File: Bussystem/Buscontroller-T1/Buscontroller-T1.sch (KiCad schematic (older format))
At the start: 14 parts, among them J1 PCIE-098-edge-conn, J2 Conn_01x02_Female, J3 J1B1211CCD, U1 LM7805L-TF3-T, U2 Teensy4.1

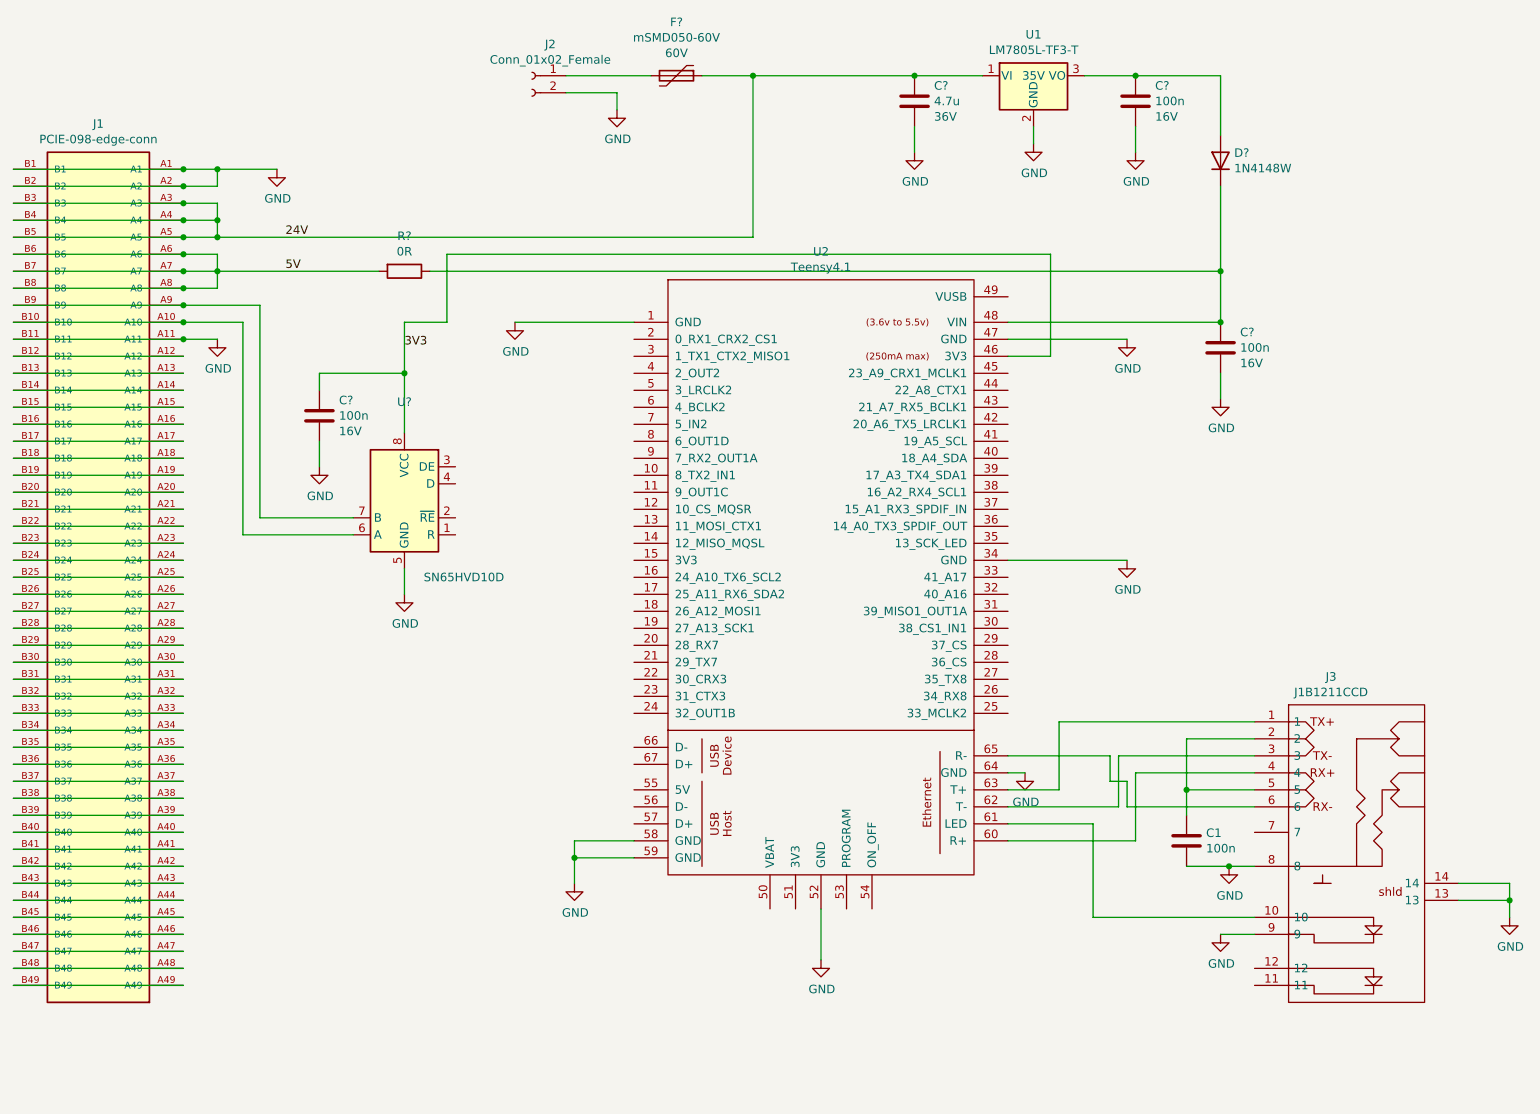
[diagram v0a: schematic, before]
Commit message: some new parts in the Buscontroller T1
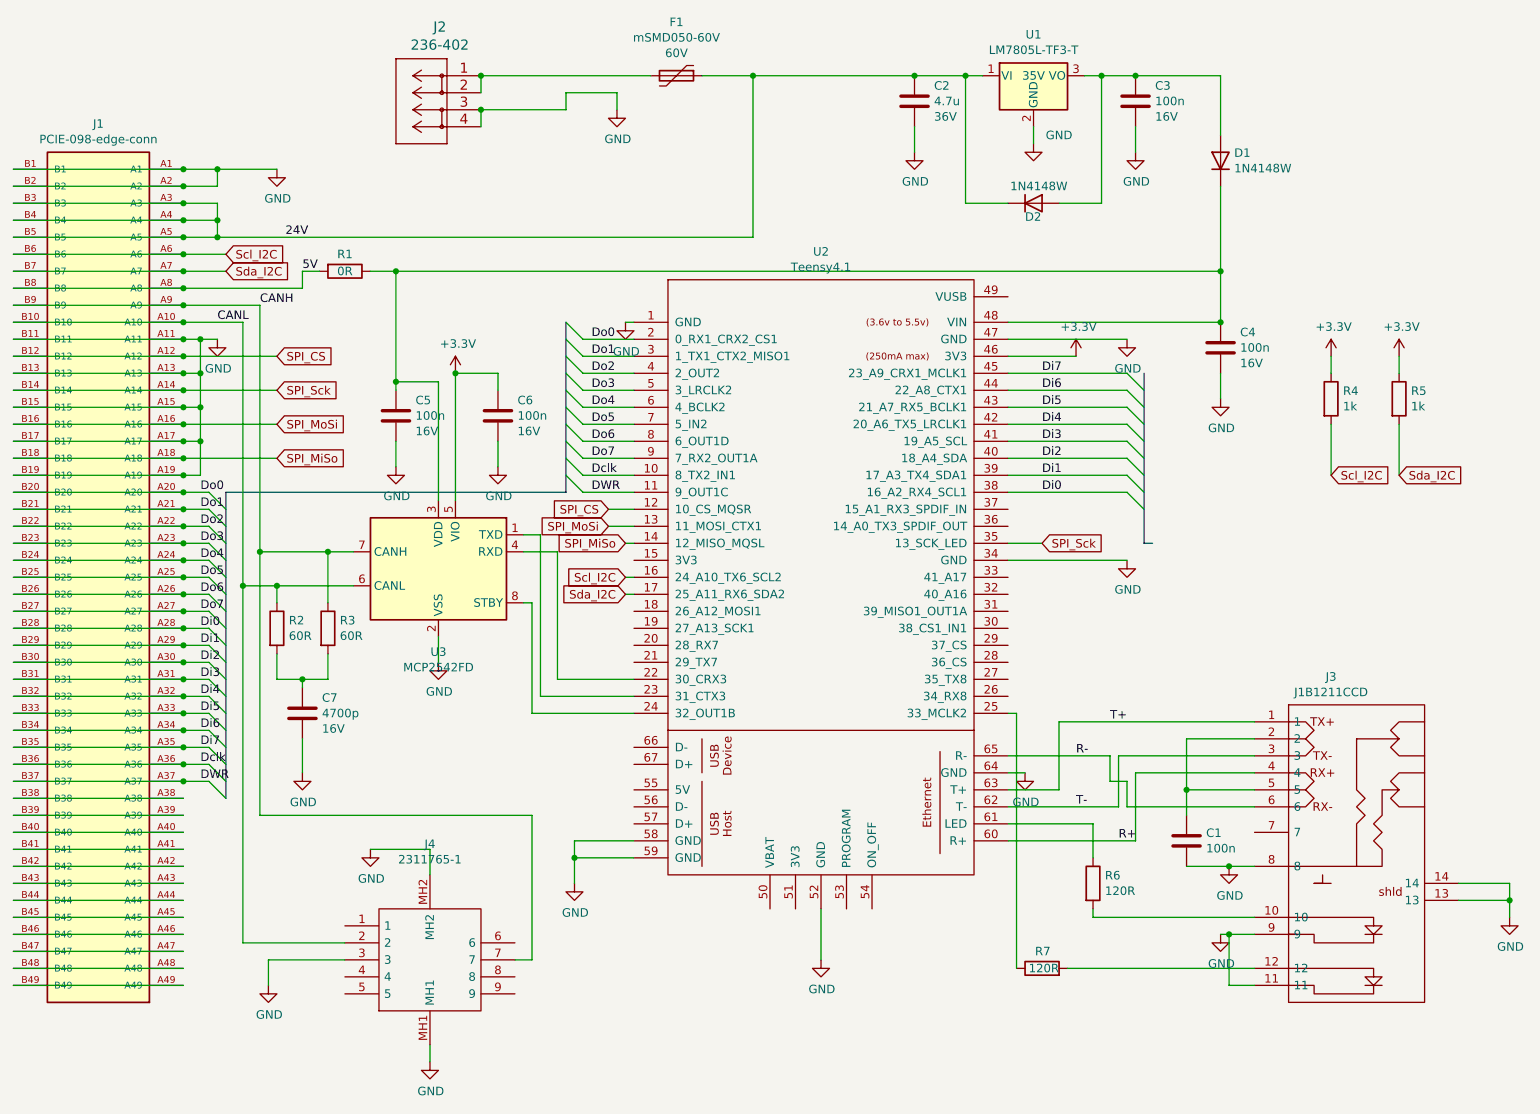
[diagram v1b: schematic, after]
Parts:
- removed J2: Conn_01x02_Female, footprints:236-402, symbol Connector:Conn_01x02_Female
- removed U?: SN65HVD10D, Package_SO:SOIC-8_3.9x4.9mm_P1.27mm, symbol Interface_UART:SN65LBC176D
- added C5: 100n, Capacitors_SMD:C_0805_HandSoldering, symbol Device:C
- added C7: 4700p, Capacitors_SMD:C_0805_HandSoldering, symbol Device:C
- added D2: 1N4148W, Diodes_SMD:D_SOD-123, symbol Device:D
- added J2: 236-402, footprints:236-402, symbol 2021-07-08_17-54-53:236-402
- added J4: 2311765-1, 23117651, symbol SamacSys_Parts:2311765-1
- added R2, R3: 60R, Resistors_SMD:R_0603_HandSoldering, symbol Device:R
- added R4, R5: 1k, Resistors_SMD:R_0603_HandSoldering, symbol Device:R
- added R6, R7: 120R, Resistors_SMD:R_0603_HandSoldering, symbol Device:R
- added U3: MCP2542FD, Housings_SOIC:SOIC-8-1EP_3.9x4.9mm_Pitch1.27mm, symbol Interface_CAN_LIN:MCP2542FDxMF
- gave numbers to parts that had none: 7
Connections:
- net 24V: now also D2.1 (K)
- net 5V: no longer J1.A6, J1.A7, J1.B6, J1.B7
- net GND: now also J1.A13, J1.A15, J1.A17, J1.A19, J1.B13, J1.B15, J1.B17, J1.B19, J3.11, C5.2, C7.2, J2.3, J2.4, J4.3, J4.MH1, J4.MH2, U3.2 (VSS), U3.9 (VSS)
- net CANL: now reaches J1.A10, J1.B10
- net CANL: now also J4.2, R2.1, U3.6 (CANL)
- net SPI_CS: now reaches J1.A12, J1.B12
- net SPI_CS: now also U2.12 (10_CS_MQSR)
- net SPI_Sck: now reaches J1.A14, J1.B14
- net SPI_Sck: now also U2.35 (13_SCK_LED)
- net SPI_MoSi: now reaches J1.A16, J1.B16
- net SPI_MoSi: now also U2.13 (11_MOSI_CTX1)
- net SPI_MiSo: now reaches J1.A18, J1.B18
- net SPI_MiSo: now also U2.14 (12_MISO_MQSL)
- net Do0: now reaches J1.A20, J1.B20
- net Do0: now also U2.2 (0_RX1_CRX2_CS1)
- net Do1: now reaches J1.A21, J1.B21
- net Do1: now also U2.3 (1_TX1_CTX2_MISO1)
- net Do2: now reaches J1.A22, J1.B22
- net Do2: now also U2.4 (2_OUT2)
- net Do3: now reaches J1.A23, J1.B23
- net Do3: now also U2.5 (3_LRCLK2)
- net Do4: now reaches J1.A24, J1.B24
- net Do4: now also U2.6 (4_BCLK2)
- net Do5: now reaches J1.A25, J1.B25
- net Do5: now also U2.7 (5_IN2)
- net Do6: now reaches J1.A26, J1.B26
- net Do6: now also U2.8 (6_OUT1D)
- net Do7: now reaches J1.A27, J1.B27
- net Do7: now also U2.9 (7_RX2_OUT1A)
- net Di0: now reaches J1.A28, J1.B28
- net Di0: now also U2.38 (16_A2_RX4_SCL1)
- net Di1: now reaches J1.A29, J1.B29
- net Di1: now also U2.39 (17_A3_TX4_SDA1)
- net Di2: now reaches J1.A30, J1.B30
- net Di2: now also U2.40 (18_A4_SDA)
- net Di3: now reaches J1.A31, J1.B31
- net Di3: now also U2.41 (19_A5_SCL)
- net Di4: now reaches J1.A32, J1.B32
- net Di4: now also U2.42 (20_A6_TX5_LRCLK1)
- net Di5: now reaches J1.A33, J1.B33
- net Di5: now also U2.43 (21_A7_RX5_BCLK1)
- net Di6: now reaches J1.A34, J1.B34
- net Di6: now also U2.44 (22_A8_CTX1)
- net Di7: now reaches J1.A35, J1.B35
- net Di7: now also U2.45 (23_A9_CRX1_MCLK1)
- net Dclk: now reaches J1.A36, J1.B36
- net Dclk: now also U2.10 (8_TX2_IN1)
- net DWR: now reaches J1.A37, J1.B37
- net DWR: now also U2.11 (9_OUT1C)
- net CANH: now reaches J1.A9, J1.B9
- net CANH: now also J4.7, R3.1, U3.7 (CANH)
- net T+: now reaches J3.1, U2.63 (T+)
- net at J3.10: now also R6.2; no longer U2.61 (LED)
- net at J3.12: now also R7.2
- net T-: now reaches J3.3, U2.62 (T-)
- net R+: now reaches J3.4, U2.60 (R+)
- net R-: now reaches J3.6, U2.65 (R-)
- net at F1.2: now also J2.1, J2.2
- net Scl_I2C: now reaches U2.16 (24_A10_TX6_SCL2)
- net Scl_I2C: now also J1.A6, J1.B6, R4.2
- net Sda_I2C: now reaches U2.17 (25_A11_RX6_SDA2)
- net Sda_I2C: now also J1.A7, J1.B7, R5.2
- net at U2.22 (30_CRX3): now also U3.4 (RXD)
- net at U2.23 (31_CTX3): now also U3.1 (TXD)
- net at U2.24 (32_OUT1B): now also U3.8 (STBY)
- net at U2.25 (33_MCLK2): now also R7.1
- net at C4.1, D1.1 (K), R1.1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: now also C5.1, U3.3 (VDD)
- net at C3.1, D1.2 (A), U1.3 (VO): now also D2.2 (A)
- net 3V3 renamed +3V3
- net +3V3: now also R4.1, R5.1, U3.5 (VIO)
- new net: R6.1, U2.61 (LED)
- new net: C7.1, R2.2, R3.2
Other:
- moved on the sheet: C6, R1

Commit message: buscontroller T1 fertig
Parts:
- removed D1: 1N4148W, Diodes_SMD:D_SOD-123, symbol Device:D
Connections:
- net +3V3: now also U2.15 (3V3)
- net D0: now reaches J1.A38, J1.B38
- net D0: now also U2.18 (26_A12_MOSI1)
- net D1: now reaches J1.A39, J1.B39
- net D1: now also U2.19 (27_A13_SCK1)
- net D2: now reaches J1.A40, J1.B40
- net D2: now also U2.20 (28_RX7)
- net D3: now reaches J1.A41, J1.B41
- net D3: now also U2.21 (29_TX7)
- net D4: now reaches J1.A42, J1.B42
- net D4: now also U2.26 (34_RX8)
- net D5: now reaches J1.A43, J1.B43
- net D5: now also U2.27 (35_TX8)
- net D6: now reaches J1.A44, J1.B44
- net D6: now also U2.28 (36_CS)
- net D7: now reaches J1.A45, J1.B45
- net D7: now also U2.29 (37_CS)
- net D8: now reaches J1.A46, J1.B46
- net D8: now also U2.30 (38_CS1_IN1)
- net D9: now reaches J1.A47, J1.B47
- net D9: now also U2.31 (39_MISO1_OUT1A)
- net D10: now reaches J1.A48, J1.B48
- net D10: now also U2.32 (40_A16)
- net D11: now reaches J1.A49, J1.B49
- net D11: now also U2.33 (41_A17)
- net CANRX3: now reaches U2.22 (30_CRX3), U3.4 (RXD)
- net CANTX3: now reaches U2.23 (31_CTX3), U3.1 (TXD)
- net CANStby: now reaches U2.24 (32_OUT1B), U3.8 (STBY)
- net at C4.1, C5.1, R1.1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: now also C3.1, D2.2 (A), U1.3 (VO)
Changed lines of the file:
@@
 	2250 5800 1250 5800
-Wire Wire Line
-	1250 5900 2250 5900
 Wire Wire Line
 	2250 6000 1250 6000
@@
 Wire Wire Line
 	7550 850  7650 850
-Wire Wire Line
-	8350 850  8350 1200
 $Comp
 L Device:C C2
@@
 	1    0    0    -1
 $EndComp
-$Comp
-L Device:D D1
-U 1 1 60EC8489
-P 8350 1350
-F 0 "D1" V 8396 1270 50  0000 R CNN
-F 1 "1N4148W" V 8305 1270 50  0000 R CNN
-F 2 "Diodes_SMD:D_SOD-123" H 8350 1350 50  0001 C CNN
-F 3 "~" H 8350 1350 50  0001 C CNN
-F 4 "C81598" H 8350 1350 50  0001 C CNN "Partnumber"
-	1    8350 1350
-	0    -1   -1   0
-$EndComp
-Wire Wire Line
-	8350 1500 8350 2000
 $Comp
 L power:GND #PWR0114
@@
 Text Label 2350 5000 0    50   ~ 0
 DWR
+Wire Wire Line
+	8350 850  8350 2000
+Text Label 4550 4400 0    50   ~ 0
+CANRX3
+Text Label 4500 4500 0    50   ~ 0
+CANTX3
+Text Label 4400 4600 0    50   ~ 0
+CANStby
+Entry Wire Line
+	4650 4100 4750 4000
+Wire Wire Line
+	4750 4000 4900 4000
+Entry Wire Line
+	4650 4150 4750 4050
+Entry Wire Line
+	4650 4250 4750 4150
+Entry Wire Line
+	4650 4350 4750 4250
+Wire Wire Line
+	4900 4050 4900 4100
+Wire Wire Line
+	4750 4050 4900 4050
+Wire Wire Line
+	4750 4150 4900 4150
+Wire Wire Line
+	4900 4150 4900 4200
+Wire Wire Line
+	4750 4250 4900 4250
+Wire Wire Line
+	4900 4250 4900 4300
+Wire Bus Line
+	4650 4350 4700 4350
+Text Label 4750 4000 0    50   ~ 0
+D0
+Text Label 4750 4050 0    50   ~ 0
+D1
+Text Label 4750 4150 0    50   ~ 0
+D2
+Text Label 4750 4250 0    50   ~ 0
+D3
+Entry Wire Line
+	7300 4500 7400 4600
+Entry Wire Line
+	7300 4400 7400 4500
+Entry Wire Line
+	7300 4300 7400 4400
+Entry Wire Line
+	7300 4200 7400 4300
+Entry Wire Line
+	7300 4100 7400 4200
+Entry Wire Line
+	7300 4000 7400 4100
+Entry Wire Line
+	7300 3900 7400 4000
+Entry Wire Line
+	7300 3800 7400 3900
+Wire Wire Line
+	7100 3800 7300 3800
+Wire Wire Line
+	7300 3900 7100 3900
+Wire Wire Line
+	7100 4000 7300 4000
+Wire Wire Line
+	7300 4100 7100 4100
+Wire Wire Line
+	7100 4200 7300 4200
+Wire Wire Line
+	7300 4300 7100 4300
+Wire Wire Line
+	7100 4400 7300 4400
+Wire Wire Line
+	7300 4500 7100 4500
+$Comp
+L power:+3.3V #PWR0128
+U 1 1 619B5A9E
+P 4750 3700
+F 0 "#PWR0128" H 4750 3550 50  0001 C CNN
+F 1 "+3.3V" H 4765 3873 50  0000 C CNN
+F 2 "" H 4750 3700 50  0001 C CNN
+F 3 "" H 4750 3700 50  0001 C CNN
+	1    4750 3700
+	0    -1   -1   0
+$EndComp
+Wire Wire Line
+	4900 3700 4750 3700
+Text Label 7150 3800 0    50   ~ 0
+D11
+Text Label 7150 4400 0    50   ~ 0
+D5
+Text Label 7150 4300 0    50   ~ 0
+D6
+Text Label 7150 4200 0    50   ~ 0
+D7
+Text Label 7150 4100 0    50   ~ 0
+D8
+Text Label 7150 4000 0    50   ~ 0
+D9
+Text Label 7150 3900 0    50   ~ 0
+D10
+Text Label 7150 4500 0    50   ~ 0
+D4
+Wire Bus Line
+	4650 5150 2450 5150
+Connection ~ 4650 4350
+Wire Bus Line
+	4650 4350 4650 5150
+Entry Wire Line
+	2350 5100 2450 5200
+Entry Wire Line
+	2350 5200 2450 5300
+Entry Wire Line
+	2350 5300 2450 5400
+Entry Wire Line
+	2350 5400 2450 5500
+Entry Wire Line
+	2350 5500 2450 5600
+Entry Wire Line
+	2350 5600 2450 5700
+Entry Wire Line
+	2350 5700 2450 5800
+Entry Wire Line
+	2350 5800 2450 5900
+Entry Wire Line
+	2350 5900 2450 6000
+Entry Wire Line
+	2350 6000 2450 6100
+Entry Wire Line
+	2350 6100 2450 6200
+Entry Wire Line
+	2350 6200 2450 6300
+Wire Wire Line
+	2350 5100 2250 5100
+Connection ~ 2250 5100
+Wire Wire Line
+	2250 5200 2350 5200
+Connection ~ 2250 5200
+Wire Wire Line
+	2350 5300 2250 5300
+Connection ~ 2250 5300
+Wire Wire Line
+	2250 5400 2350 5400
+Connection ~ 2250 5400
+Wire Wire Line
+	2350 5500 2250 5500
+Connection ~ 2250 5500
+Wire Wire Line
+	2250 5600 2350 5600
+Connection ~ 2250 5600
+Wire Wire Line
+	2350 5700 2250 5700
+Connection ~ 2250 5700
+Wire Wire Line
+	2250 5800 2350 5800
+Connection ~ 2250 5800
+Wire Wire Line
+	1250 5900 2250 5900
+Connection ~ 2250 5900
+Wire Wire Line
+	2250 5900 2350 5900
+Wire Wire Line
+	2250 6000 2350 6000
+Connection ~ 2250 6000
+Wire Wire Line
+	2350 6100 2250 6100
+Connection ~ 2250 6100
+Wire Wire Line
+	2250 6200 2350 6200
+Connection ~ 2250 6200
+Text Label 2350 5100 0    50   ~ 0
+D0
+Text Label 2350 5200 0    50   ~ 0
+D1
+Text Label 2350 5300 0    50   ~ 0
+D2
+Text Label 2350 5400 0    50   ~ 0
+D3
+Text Label 2350 5500 0    50   ~ 0
+D4
+Text Label 2350 5600 0    50   ~ 0
+D5
+Text Label 2350 5700 0    50   ~ 0
+D6
+Text Label 2350 5800 0    50   ~ 0
+D7
+Text Label 2350 5900 0    50   ~ 0
+D8
+Text Label 2350 6000 0    50   ~ 0
+D9
+Text Label 2350 6100 0    50   ~ 0
+D10
+Text Label 2350 6200 0    50   ~ 0
+D11
+Wire Bus Line
+	4650 4000 4650 4350
 Wire Bus Line
 	7900 2600 7900 3600
@@
 	4500 2300 4500 3300
 Wire Bus Line
+	7400 3800 7400 4600
+Wire Bus Line
+	2450 5150 2450 6300
+Wire Bus Line
 	2500 3300 2500 5100
